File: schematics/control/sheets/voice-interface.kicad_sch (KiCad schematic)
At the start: 1 part

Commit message: Added pulse width mod schematics
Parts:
- renumbered J_VOICE1 to J_VOICE2
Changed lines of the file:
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@@
   (symbol (lib_id "power:-12V") (at 111.76 67.31 180) (unit 1)
     (in_bom yes) (on_board yes) (dnp no) (fields_autoplaced)
-    (property "Reference" "#PWR02" (at 111.76 69.85 0)
+    (property "Reference" "#PWR059" (at 111.76 69.85 0)
       (effects (font (size 1.27 1.27)) hide)
     )
@@
       (project "shmoergh-funk-live-control"
         (path "/6d7b782d-8b2e-4b40-a99f-4bf41187d978/fae2190e-fad4-442c-a22e-78ec22052747"
-          (reference "#PWR02") (unit 1)
+          (reference "#PWR059") (unit 1)
         )
         (path "/6d7b782d-8b2e-4b40-a99f-4bf41187d978/b7a699bc-9ede-4e43-9489-973cb040f68d"
-          (reference "#PWR01") (unit 1)
+          (reference "#PWR013") (unit 1)
         )
         (path "/6d7b782d-8b2e-4b40-a99f-4bf41187d978/73026543-dc8b-456d-a908-7f59f5614f87"
-          (reference "#PWR03") (unit 1)
+          (reference "#PWR066") (unit 1)
         )
         (path "/6d7b782d-8b2e-4b40-a99f-4bf41187d978/353d5b2a-c681-4771-a3eb-42d12aea31d6"
-          (reference "#PWR04") (unit 1)
+          (reference "#PWR069") (unit 1)
         )
         (path "/6d7b782d-8b2e-4b40-a99f-4bf41187d978/6fe26819-ddf5-49d3-9f61-5b33d8ddd23b"
-          (reference "#PWR05") (unit 1)
+          (reference "#PWR072") (unit 1)
         )
         (path "/6d7b782d-8b2e-4b40-a99f-4bf41187d978/b522819c-7318-464a-82c8-e9514cdb3472"
-          (reference "#PWR06") (unit 1)
+          (reference "#PWR083") (unit 1)
         )
       )
@@
   (symbol (lib_id "power:GND") (at 106.68 67.31 0) (unit 1)
     (in_bom yes) (on_board yes) (dnp no) (fields_autoplaced)
-    (property "Reference" "#PWR08" (at 106.68 73.66 0)
+    (property "Reference" "#PWR058" (at 106.68 73.66 0)
       (effects (font (size 1.27 1.27)) hide)
     )
@@
       (project "shmoergh-funk-live-control"
         (path "/6d7b782d-8b2e-4b40-a99f-4bf41187d978/fae2190e-fad4-442c-a22e-78ec22052747"
-          (reference "#PWR08") (unit 1)
+          (reference "#PWR058") (unit 1)
         )
         (path "/6d7b782d-8b2e-4b40-a99f-4bf41187d978/b7a699bc-9ede-4e43-9489-973cb040f68d"
-          (reference "#PWR07") (unit 1)
+          (reference "#PWR012") (unit 1)
         )
         (path "/6d7b782d-8b2e-4b40-a99f-4bf41187d978/73026543-dc8b-456d-a908-7f59f5614f87"
-          (reference "#PWR09") (unit 1)
+          (reference "#PWR065") (unit 1)
         )
         (path "/6d7b782d-8b2e-4b40-a99f-4bf41187d978/353d5b2a-c681-4771-a3eb-42d12aea31d6"
-          (reference "#PWR010") (unit 1)
+          (reference "#PWR068") (unit 1)
         )
         (path "/6d7b782d-8b2e-4b40-a99f-4bf41187d978/6fe26819-ddf5-49d3-9f61-5b33d8ddd23b"
-          (reference "#PWR011") (unit 1)
+          (reference "#PWR071") (unit 1)
         )
         (path "/6d7b782d-8b2e-4b40-a99f-4bf41187d978/b522819c-7318-464a-82c8-e9514cdb3472"
-          (reference "#PWR012") (unit 1)
+          (reference "#PWR082") (unit 1)
         )
       )
@@
   (symbol (lib_id "Connector_Generic:Conn_01x11") (at 138.43 73.66 0) (unit 1)
     (in_bom yes) (on_board yes) (dnp no) (fields_autoplaced)
-    (property "Reference" "J_VOICE1" (at 140.97 73.025 0)
+    (property "Reference" "J_VOICE2" (at 140.97 73.025 0)
       (effects (font (size 1.27 1.27)) (justify left))
     )
@@
       (project "shmoergh-funk-live-control"
         (path "/6d7b782d-8b2e-4b40-a99f-4bf41187d978/fae2190e-fad4-442c-a22e-78ec22052747"
-          (reference "J_VOICE1") (unit 1)
+          (reference "J_VOICE2") (unit 1)
         )
         (path "/6d7b782d-8b2e-4b40-a99f-4bf41187d978/b7a699bc-9ede-4e43-9489-973cb040f68d"
-          (reference "J_VOICE2") (unit 1)
+          (reference "J_VOICE1") (unit 1)
         )
         (path "/6d7b782d-8b2e-4b40-a99f-4bf41187d978/73026543-dc8b-456d-a908-7f59f5614f87"
@@
   (symbol (lib_id "power:+12V") (at 130.81 59.69 0) (unit 1)
     (in_bom yes) (on_board yes) (dnp no) (fields_autoplaced)
-    (property "Reference" "#PWR014" (at 130.81 63.5 0)
+    (property "Reference" "#PWR060" (at 130.81 63.5 0)
       (effects (font (size 1.27 1.27)) hide)
     )
@@
       (project "shmoergh-funk-live-control"
         (path "/6d7b782d-8b2e-4b40-a99f-4bf41187d978/fae2190e-fad4-442c-a22e-78ec22052747"
+          (reference "#PWR060") (unit 1)
+        )
+        (path "/6d7b782d-8b2e-4b40-a99f-4bf41187d978/b7a699bc-9ede-4e43-9489-973cb040f68d"
           (reference "#PWR014") (unit 1)
         )
-        (path "/6d7b782d-8b2e-4b40-a99f-4bf41187d978/b7a699bc-9ede-4e43-9489-973cb040f68d"
-          (reference "#PWR013") (unit 1)
-        )
         (path "/6d7b782d-8b2e-4b40-a99f-4bf41187d978/73026543-dc8b-456d-a908-7f59f5614f87"
-          (reference "#PWR015") (unit 1)
+          (reference "#PWR067") (unit 1)
         )
         (path "/6d7b782d-8b2e-4b40-a99f-4bf41187d978/353d5b2a-c681-4771-a3eb-42d12aea31d6"
-          (reference "#PWR016") (unit 1)
+          (reference "#PWR070") (unit 1)
         )
         (path "/6d7b782d-8b2e-4b40-a99f-4bf41187d978/6fe26819-ddf5-49d3-9f61-5b33d8ddd23b"
-          (reference "#PWR017") (unit 1)
+          (reference "#PWR073") (unit 1)
         )
         (path "/6d7b782d-8b2e-4b40-a99f-4bf41187d978/b522819c-7318-464a-82c8-e9514cdb3472"
-          (reference "#PWR018") (unit 1)
+          (reference "#PWR084") (unit 1)
         )
       )

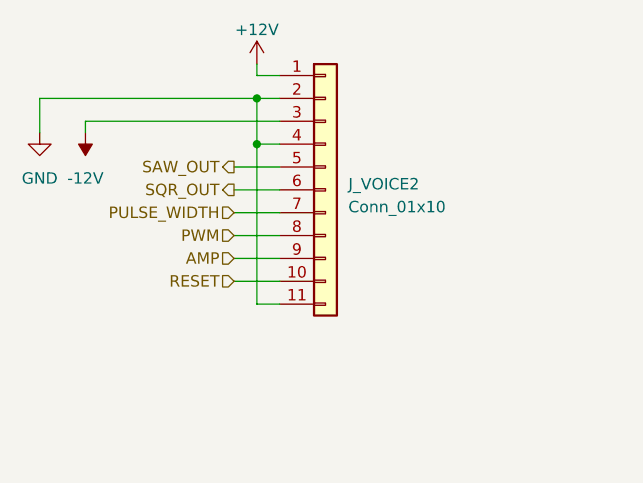
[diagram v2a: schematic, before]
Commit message: Added all UI components to schematics
- digital UI
- filter UI
- updated voice interface connection
- simplified schematics a lot
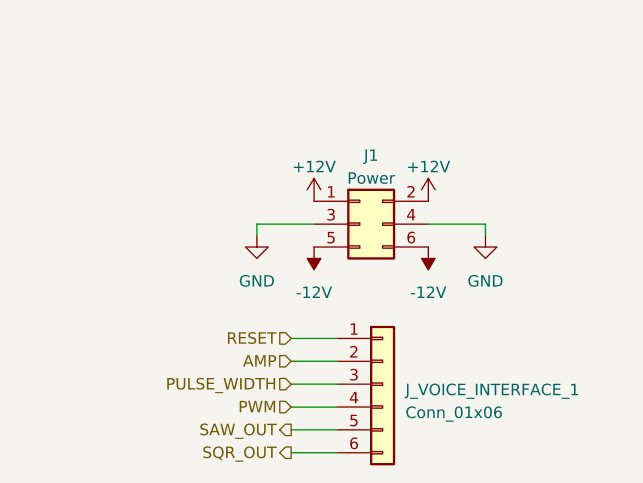
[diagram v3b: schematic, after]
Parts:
- removed J_VOICE2: Conn_01x10, Connector_PinSocket_2.54mm:PinSocket_1x11_P2.54mm_Vertical, symbol Connector_Generic:Conn_01x11
- added J1: Power, Connector_PinHeader_2.54mm:PinHeader_2x03_P2.54mm_Vertical, symbol Connector_Generic:Conn_02x03_Odd_Even
- added J_VOICE_INTERFACE_1: Conn_01x06, Connector_PinHeader_2.54mm:PinHeader_1x06_P2.54mm_Vertical, symbol Connector_Generic:Conn_01x06
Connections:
- net +12V: now also J1.1 (Pin_1), J1.2 (Pin_2)
- net -12V: now also J1.5 (Pin_5), J1.6 (Pin_6)
- net AMP: now also J_VOICE_INTERFACE_1.2 (Pin_2)
- net GND: now also J1.3 (Pin_3), J1.4 (Pin_4)
- net PULSE_WIDTH: now also J_VOICE_INTERFACE_1.3 (Pin_3)
- net PWM: now also J_VOICE_INTERFACE_1.4 (Pin_4)
- net RESET: now also J_VOICE_INTERFACE_1.1 (Pin_1)
- net SAW_OUT: now also J_VOICE_INTERFACE_1.5 (Pin_5)
- net SQR_OUT: now also J_VOICE_INTERFACE_1.6 (Pin_6)

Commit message: Schemo work
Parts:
- renumbered J1 to J?, J_VOICE_INTERFACE_1 to J_VOICE_INTERFACE_?
